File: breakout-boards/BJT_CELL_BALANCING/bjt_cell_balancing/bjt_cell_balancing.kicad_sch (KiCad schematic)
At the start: 14 parts, among them Q1 DNBT8105-7, SW1 SW_SPST

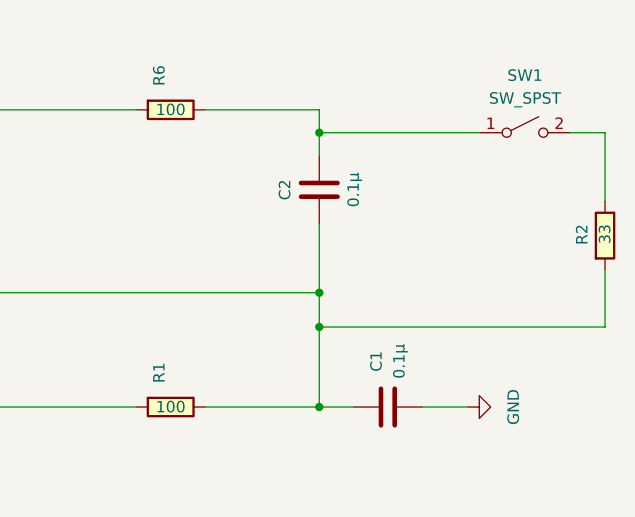
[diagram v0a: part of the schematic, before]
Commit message: feat: changed cell balancing schem
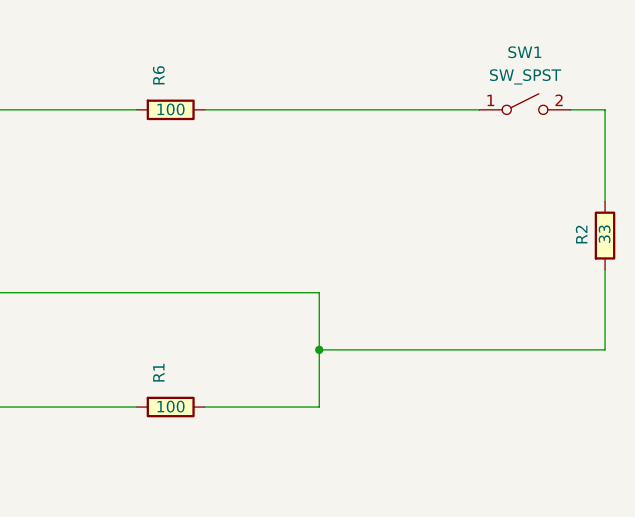
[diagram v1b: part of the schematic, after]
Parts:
- removed C1, C2: 0.1µ, FixedWing:CAP_GCJ-18_MUR, symbol FixedWing:GCJ188R72A104KA01D
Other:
- moved on the sheet: SW1
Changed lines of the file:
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@@
 (kicad_sch (version 20230121) (generator eeschema)
   (paper "A4")
-  (junction (at 200.66 106.68) (diameter 0) (color 0 0 0 0)
-  )
   (junction (at 97.79 92.71) (diameter 0) (color 0 0 0 0)
   )
@@
   (junction (at 97.79 82.55) (diameter 0) (color 0 0 0 0)
   )
-  (junction (at 200.66 85.09) (diameter 0) (color 0 0 0 0)
-  )
   (junction (at 82.55 92.71) (diameter 0) (color 0 0 0 0)
   )
@@
   (junction (at 105.41 82.55) (diameter 0) (color 0 0 0 0)
   )
-  (junction (at 200.66 115.57) (diameter 0) (color 0 0 0 0)
-  )
-  (junction (at 200.66 102.87) (diameter 0) (color 0 0 0 0)
-  )
   (junction (at 105.41 92.71) (diameter 0) (color 0 0 0 0)
   )
-  (wire (pts (xy 232.41 106.68) (xy 200.66 106.68))
+  (junction (at 200.66 109.22) (diameter 0) (color 0 0 0 0)
+  )
+  (wire (pts (xy 232.41 109.22) (xy 200.66 109.22))
     (stroke (width 0) (type default))
   )
@@
     (stroke (width 0) (type default))
   )
-  (wire (pts (xy 200.66 85.09) (xy 200.66 87.63))
-    (stroke (width 0) (type default))
-  )
   (wire (pts (xy 82.55 115.57) (xy 82.55 119.38))
     (stroke (width 0) (type default))
@@
     (stroke (width 0) (type default))
   )
-  (wire (pts (xy 232.41 85.09) (xy 232.41 92.71))
+  (wire (pts (xy 232.41 82.55) (xy 232.41 92.71))
     (stroke (width 0) (type default))
   )
@@
     (stroke (width 0) (type default))
   )
-  (wire (pts (xy 204.47 115.57) (xy 200.66 115.57))
-    (stroke (width 0) (type default))
-  )
   (wire (pts (xy 97.79 91.44) (xy 97.79 92.71))
     (stroke (width 0) (type default))
@@
     (stroke (width 0) (type default))
   )
-  (wire (pts (xy 187.96 82.55) (xy 200.66 82.55))
+  (wire (pts (xy 200.66 102.87) (xy 200.66 109.22))
     (stroke (width 0) (type default))
   )
@@
     (stroke (width 0) (type default))
   )
-  (wire (pts (xy 200.66 82.55) (xy 200.66 85.09))
+  (wire (pts (xy 187.96 82.55) (xy 218.44 82.55))
     (stroke (width 0) (type default))
   )
@@
     (stroke (width 0) (type default))
   )
-  (wire (pts (xy 232.41 85.09) (xy 228.6 85.09))
-    (stroke (width 0) (type default))
-  )
-  (wire (pts (xy 200.66 106.68) (xy 200.66 102.87))
+  (wire (pts (xy 232.41 82.55) (xy 228.6 82.55))
     (stroke (width 0) (type default))
   )
@@
     (stroke (width 0) (type default))
   )
-  (wire (pts (xy 232.41 100.33) (xy 232.41 106.68))
+  (wire (pts (xy 232.41 100.33) (xy 232.41 109.22))
     (stroke (width 0) (type default))
   )
@@
     (stroke (width 0) (type default))
   )
-  (wire (pts (xy 200.66 102.87) (xy 200.66 95.25))
-    (stroke (width 0) (type default))
-  )
-  (wire (pts (xy 200.66 85.09) (xy 218.44 85.09))
-    (stroke (width 0) (type default))
-  )
   (wire (pts (xy 82.55 115.57) (xy 180.34 115.57))
     (stroke (width 0) (type default))
@@
     (stroke (width 0) (type default))
   )
-  (wire (pts (xy 200.66 115.57) (xy 200.66 106.68))
+  (wire (pts (xy 200.66 115.57) (xy 200.66 109.22))
     (stroke (width 0) (type default))
   )
@@
     (stroke (width 0) (type default))
   )
-  (wire (pts (xy 212.09 115.57) (xy 217.17 115.57))
-    (stroke (width 0) (type default))
-  )
   (wire (pts (xy 124.46 82.55) (xy 124.46 83.82))
     (stroke (width 0) (type default))
@@
     )
   )
-  (symbol (lib_id "Switch:SW_SPST") (at 223.52 85.09 0) (unit 1)
+  (symbol (lib_id "Switch:SW_SPST") (at 223.52 82.55 0) (unit 1)
     (in_bom yes) (on_board yes) (dnp no) (fields_autoplaced)
-    (property "Reference" "SW1" (at 223.52 78.74 0)
+    (property "Reference" "SW1" (at 223.52 76.2 0)
       (effects (font (size 1.27 1.27)))
     )
-    (property "Value" "SW_SPST" (at 223.52 81.28 0)
+    (property "Value" "SW_SPST" (at 223.52 78.74 0)
       (effects (font (size 1.27 1.27)))
     )
-    (property "Footprint" "" (at 223.52 85.09 0)
+    (property "Footprint" "" (at 223.52 82.55 0)
       (effects (font (size 1.27 1.27)) hide)
     )
-    (property "Datasheet" "~" (at 223.52 85.09 0)
+    (property "Datasheet" "~" (at 223.52 82.55 0)
       (effects (font (size 1.27 1.27)) hide)
     )
@@
         (path "/4ef823a3-f90b-4f75-9243-17e2a5ea7359"
           (reference "LED1") (unit 1)
-        )
-      )
-    )
-  )
-  (symbol (lib_id "FixedWing:GCJ188R72A104KA01D") (at 200.66 87.63 270) (unit 1)
-    (in_bom yes) (on_board yes) (dnp no)
-    (property "Reference" "C2" (at 196.85 91.44 0)
-      (effects (font (size 1.27 1.27)))
-    )
-    (property "Value" "0.1µ" (at 204.47 91.44 0)
-      (effects (font (size 1.27 1.27)))
-    )
-    (property "Footprint" "FixedWing:CAP_GCJ-18_MUR" (at 212.09 85.09 0)
-      (effects (font (size 1.27 1.27) italic) hide)
-    )
-    (property "Datasheet" "https://search.murata.co.jp/Ceramy/image/img/A01X/G101/ENG/GCJ21BR71A106KE01-01A.pdf" (at 212.09 85.09 0)
-      (effects (font (size 1.27 1.27) italic) hide)
-    )
-    (property "Manufacturer" "Murata Electronics" (at 212.09 86.36 0)
-      (effects (font (size 1.27 1.27)) hide)
-    )
-    (property "Manufacturer Part Number" "GCJ188R72A104KA01D" (at 212.09 85.09 0)
-      (effects (font (size 1.27 1.27)) hide)
-    )
-    (pin "1")
-    (pin "2")
-    (instances
-      (project "bjt_cell_balancing"
-        (path "/4ef823a3-f90b-4f75-9243-17e2a5ea7359"
-          (reference "C2") (unit 1)
-        )
-      )
-    )
-  )
-  (symbol (lib_id "power:GND") (at 217.17 115.57 90) (unit 1)
-    (in_bom yes) (on_board yes) (dnp no) (fields_autoplaced)
-    (property "Reference" "#PWR01" (at 223.52 115.57 0)
-      (effects (font (size 1.27 1.27)) hide)
-    )
-    (property "Value" "GND" (at 222.25 115.57 0)
-      (effects (font (size 1.27 1.27)))
-    )
-    (property "Footprint" "" (at 217.17 115.57 0)
-      (effects (font (size 1.27 1.27)) hide)
-    )
-    (property "Datasheet" "" (at 217.17 115.57 0)
-      (effects (font (size 1.27 1.27)) hide)
-    )
-    (pin "1")
-    (instances
-      (project "bjt_cell_balancing"
-        (path "/4ef823a3-f90b-4f75-9243-17e2a5ea7359"
-          (reference "#PWR01") (unit 1)
         )
       )
@@
         )
       )
-    )
-  )
-  (symbol (lib_id "FixedWing:GCJ188R72A104KA01D") (at 212.09 115.57 180) (unit 1)
-    (in_bom yes) (on_board yes) (dnp no)
-    (property "Reference" "C1" (at 207.01 110.49 90)
-      (effects (font (size 1.27 1.27)))
-    )
-    (property "Value" "0.1µ" (at 209.55 110.49 90)
-      (effects (font (size 1.27 1.27)))
-    )
-    (property "Footprint" "FixedWing:CAP_GCJ-18_MUR" (at 214.63 127 0)
-      (effects (font (size 1.27 1.27) italic) hide)
-    )
-    (property "Datasheet" "https://search.murata.co.jp/Ceramy/image/img/A01X/G101/ENG/GCJ21BR71A106KE01-01A.pdf" (at 214.63 127 0)
-      (effects (font (size 1.27 1.27) italic) hide)
-    )
-    (property "Manufacturer" "Murata Electronics" (at 213.36 127 0)
-      (effects (font (size 1.27 1.27)) hide)
-    )
-    (property "Manufacturer Part Number" "GCJ188R72A104KA01D" (at 214.63 127 0)
-      (effects (font (size 1.27 1.27)) hide)
-    )
-    (pin "1")
-    (pin "2")
-    (instances
-      (project "bjt_cell_balancing"
-        (path "/4ef823a3-f90b-4f75-9243-17e2a5ea7359"
-          (reference "C1") (unit 1)
-        )
-      )

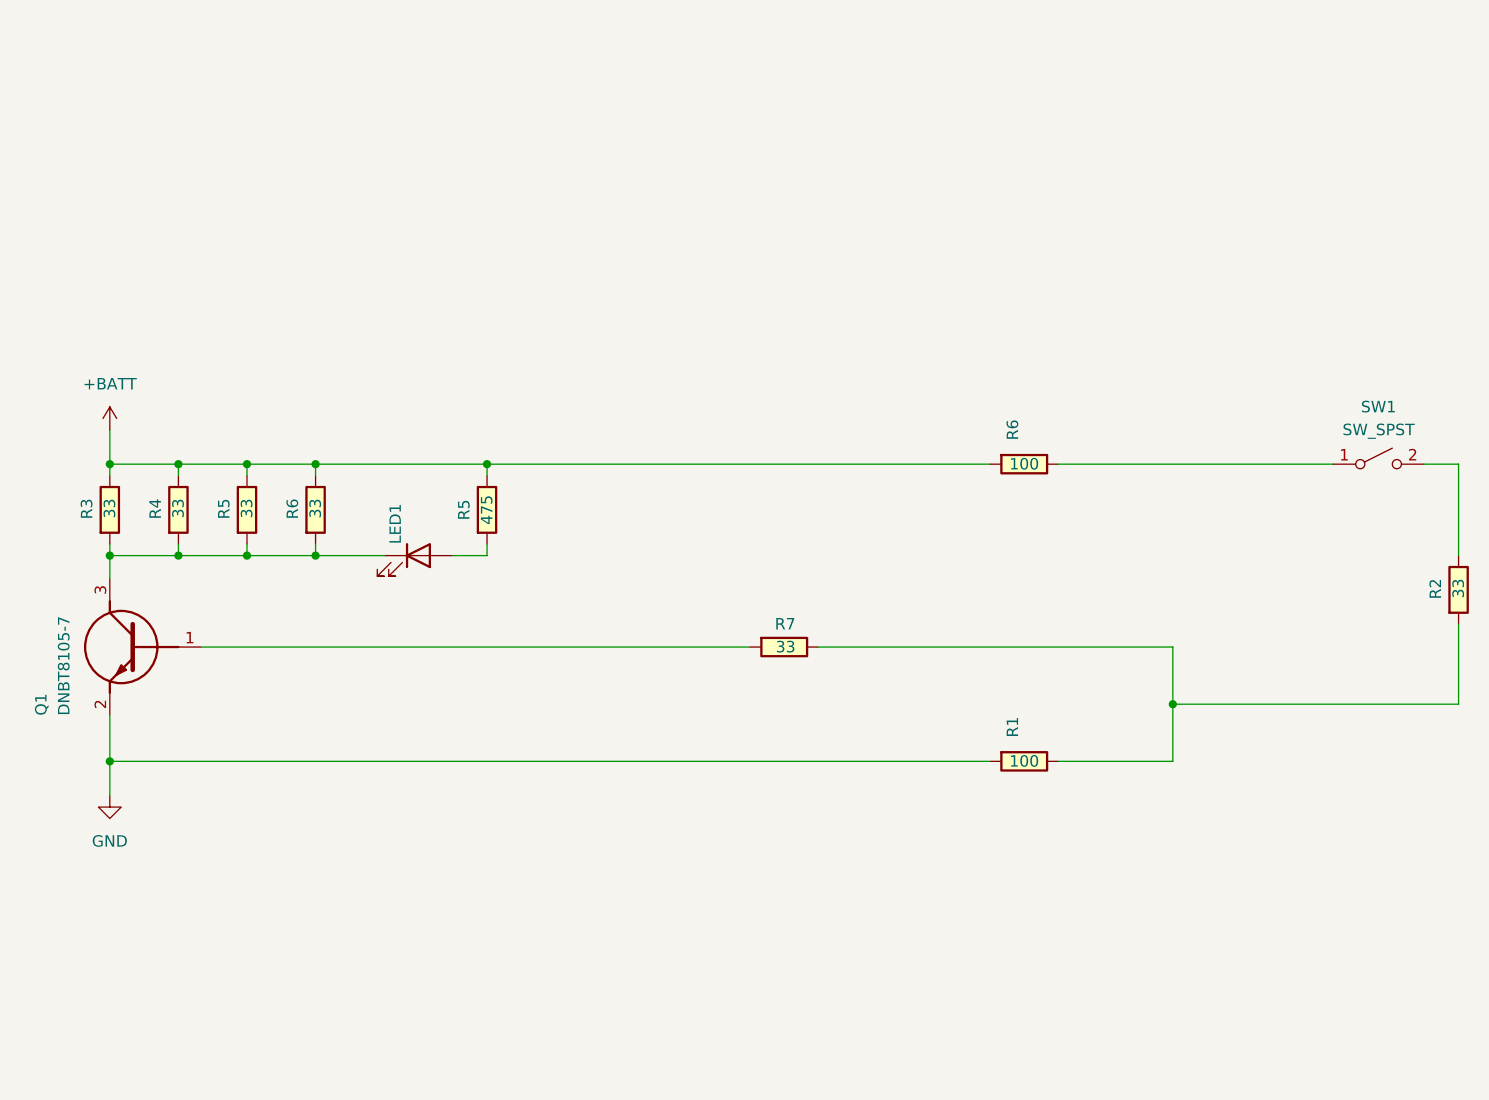
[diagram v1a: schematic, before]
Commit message: feat: slightly edited cell balance schem
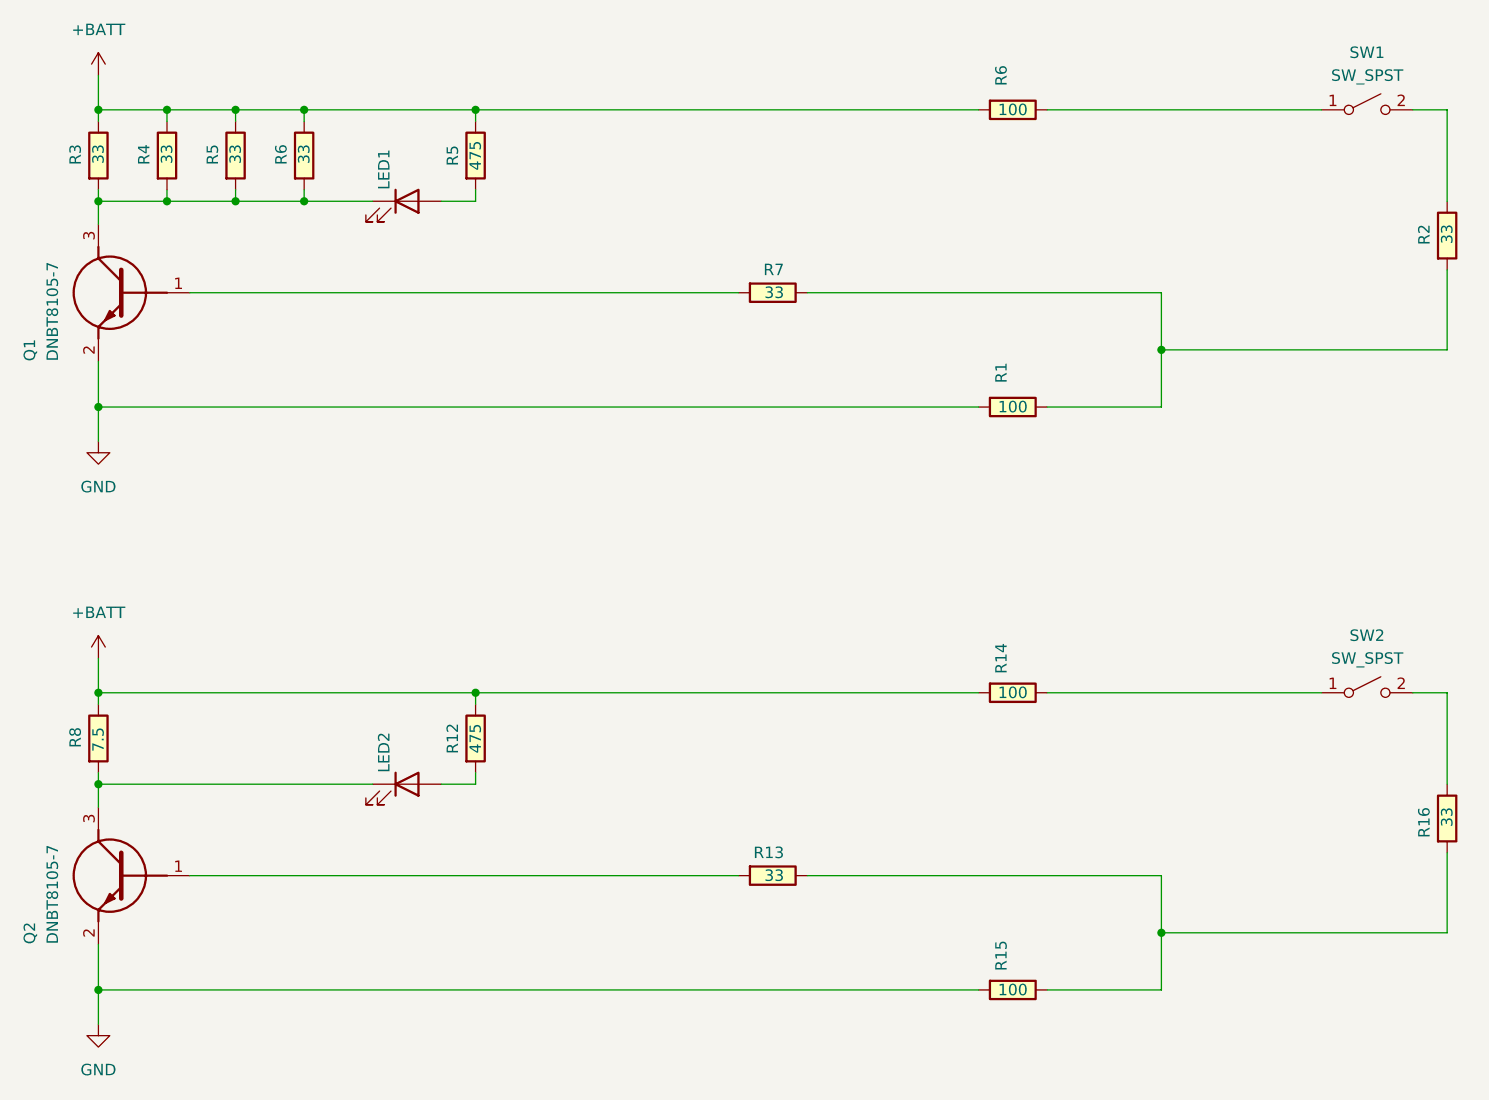
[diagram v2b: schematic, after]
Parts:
- added LED2: LTST-C170KRKT, LEDC2012X120N, symbol FixedWing:LTST-C170KRKT
- added Q2: DNBT8105-7, FixedWing:SOT95P240X105-3N, symbol FixedWing:DNBT8105-7
- added R12: 475, RESC2012X50N, symbol FixedWing:CRCW0805475RFKEA
- added R13, R16: 33, FixedWing:RC2512N_VIS, symbol Fixed Wing:CRCW251233R0FKEG
- added R14, R15: 100, RESC2012X50N, symbol FixedWing:CRCW0805100RFKEA
- added R8: 7.5, FixedWing:RC2512N_VIS, symbol Fixed Wing:CRCW251233R0FKEG
- added SW2: SW_SPST, symbol Switch:SW_SPST
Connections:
- net +BATT: now also R12.2, R14.1, R8.2
- net GND: now also Q2.2 (E), R15.1
- new net: R14.2, SW2.1 (A)
- new net: R16.2, SW2.2 (B)
- new net: LED2.1 (K), Q2.3 (C), R8.1
- new net: LED2.2 (A), R12.1
- new net: R13.2, R15.2, R16.1
- new net: Q2.1 (B), R13.1
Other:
- moved on the sheet: LED1, Q1, R1, R2, R3, R4, R5, R6, R7, SW1
